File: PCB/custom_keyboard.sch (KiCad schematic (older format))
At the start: 401 parts, among them J1 Conn_01x08_Male, SW1 M1, SW10 LSHIFT, SW11 LCTRL, SW12 1, SW13 Q, SW14 A, SW15 Z, SW16 LGUI, SW17 F1, SW18 2, SW19 W, SW2 M2, SW20 S, SW21 X, SW22 LALT, SW23 F2, SW24 3, SW25 E, SW26 D, SW27 C, SW28 F3, SW29 4, SW3 M3, SW30 R, SW31 F, SW32 V, SW33 F4, SW34 5, SW35 T, SW36 G, SW37 B, SW38 SPACE, SW39 F5, SW4 M4, SW40 6, SW41 Y, SW42 H, SW43 N, SW44 F6, SW45 7, SW46 U, SW47 J, SW48 M, SW49 F7, SW5 M5, SW50 8, SW51 I, SW52 K, SW53 ,/<, SW54 F8, SW55 9, SW56 O, SW57 L, SW58 ./>, SW59 RALT, SW6 ESC, SW60 F9, SW61 0, SW62 P, SW63 ;/:, SW64 /, SW65 RGUI, SW66 F10, SW67 -/_, SW68 [/{, SW69 '/\", SW7 `/~, SW70 CherryMX, SW71 F11, SW72 =/+, SW73 ]/}, SW74 MENU, SW75 F12, SW76 BACKSPACE, SW77 \\, SW78 ENTER, SW79 RSHIFT, SW8 TAB, SW80 RCTRL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

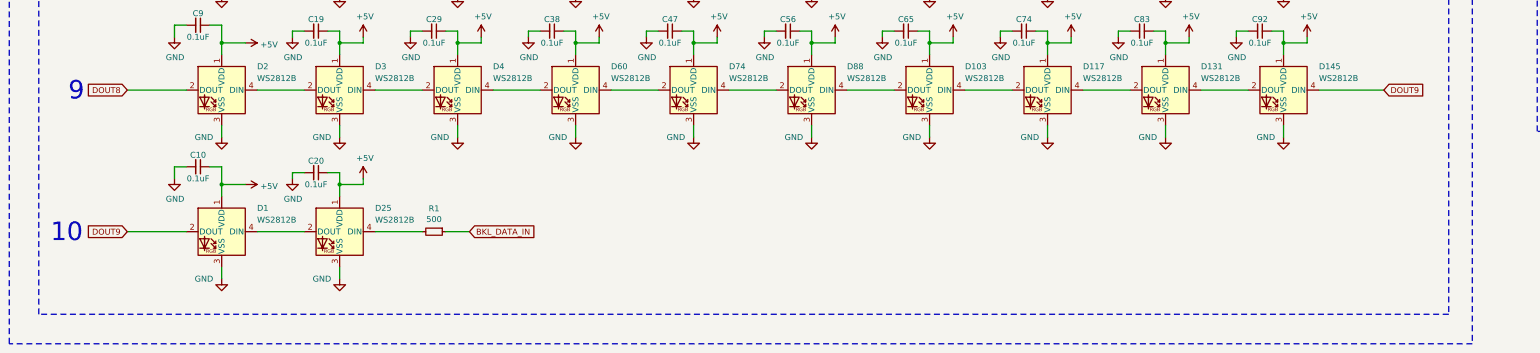
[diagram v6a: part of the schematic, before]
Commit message: Removed unnecessary lighting
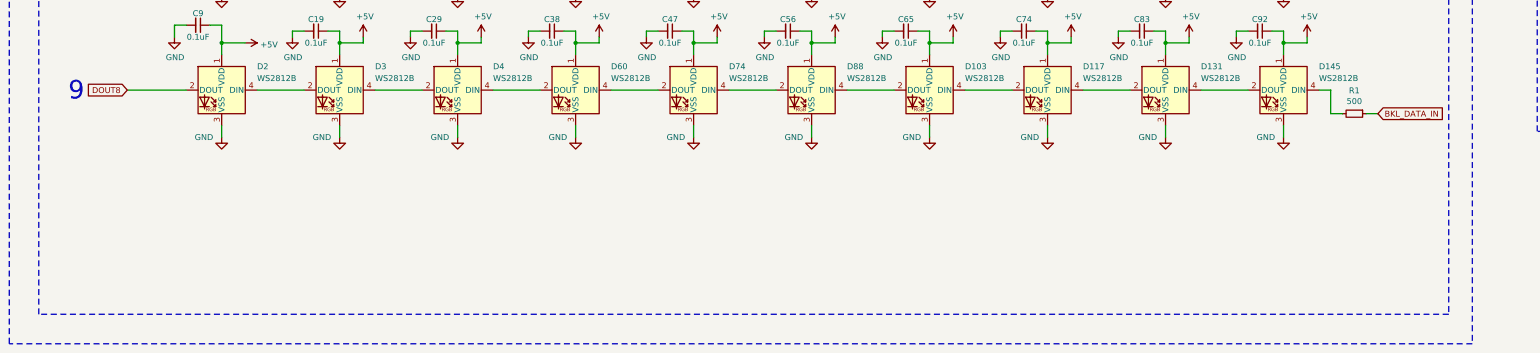
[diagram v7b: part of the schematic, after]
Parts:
- removed C10, C20: 0.1uF, symbol Device:C_Small
- removed D1, D25: WS2812B, LED_SMD:LED_WS2812B_PLCC4_5.0x5.0mm_P3.2mm, symbol LED:WS2812B
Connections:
- net DOUT9 is gone; now on an unnamed net: D145.4 (DIN)
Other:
- moved on the sheet: R1
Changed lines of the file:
@@
 Wire Notes Line
 	1200 7750 1200 1700
-Wire Wire Line
-	4450 19900 4050 19900
-Wire Wire Line
-	4850 19900 4650 19900
 $Comp
 L Device:R_Small R1
 U 1 1 68D631B8
-P 4550 19900
-F 0 "R1" V 4354 19900 50  0000 C CNN
-F 1 "500" V 4445 19900 50  0000 C CNN
-F 2 "" H 4550 19900 50  0001 C CNN
-F 3 "~" H 4550 19900 50  0001 C CNN
-	1    4550 19900
+P 12350 18900
+F 0 "R1" V 12154 18900 50  0000 C CNN
+F 1 "500" V 12245 18900 50  0000 C CNN
+F 2 "" H 12350 18900 50  0001 C CNN
+F 3 "~" H 12350 18900 50  0001 C CNN
+	1    12350 18900
 	0    1    1    0
 $EndComp
-Text GLabel 4850 19900 2    50   Input ~ 0
+Text GLabel 12550 18900 2    50   Input ~ 0
 BKL_DATA_IN
-$Comp
-L power:GND #PWR0397
-U 1 1 68D631C0
-P 3750 20300
-F 0 "#PWR0397" H 3750 20050 50  0001 C CNN
-F 1 "GND" H 3600 20300 50  0000 C CNN
-F 2 "" H 3750 20300 50  0001 C CNN
-F 3 "" H 3750 20300 50  0001 C CNN
-	1    3750 20300
-	1    0    0    -1
-$EndComp
-Wire Wire Line
-	3650 19400 3750 19400
-Wire Wire Line
-	3350 19400 3450 19400
-$Comp
-L Device:C_Small C20
-U 1 1 68D631CC
-P 3550 19400
-F 0 "C20" V 3450 19400 50  0000 C CNN
-F 1 "0.1uF" V 3650 19400 50  0000 C CNN
-F 2 "" H 3550 19400 50  0001 C CNN
-F 3 "~" H 3550 19400 50  0001 C CNN
-	1    3550 19400
-	0    1    1    0
-$EndComp
-$Comp
-L LED:WS2812B D25
-U 1 1 68D631DE
-P 3750 19900
-F 0 "D25" H 3450 20100 50  0000 R CNN
-F 1 "WS2812B" H 3450 20000 50  0000 R CNN
-F 2 "LED_SMD:LED_WS2812B_PLCC4_5.0x5.0mm_P3.2mm" H 3800 19600 50  0001 L TNN
-F 3 "https://cdn-shop.adafruit.com/datasheets/WS2812B.pdf" H 3850 19525 50  0001 L TNN
-	1    3750 19900
-	-1   0    0    -1
-$EndComp
-Text GLabel 1950 19900 0    50   Input ~ 0
-DOUT9
 Text GLabel 1950 18700 0    50   Input ~ 0
 DOUT8
@@
 Text GLabel 1950 10300 0    50   Input ~ 0
 DOUT1
-Text GLabel 12600 18700 2    50   Input ~ 0
-DOUT9
 Text GLabel 12600 17500 2    50   Input ~ 0
 DOUT8
@@
 Text Notes 1450 18800 0    157  ~ 0
 9
-Text Notes 1300 20000 0    157  ~ 0
-10\n
 Text Notes 2650 8300 0    157  ~ 0
 1
@@
 	17950 14750 17450 14750
 Wire Wire Line
-	17450 14850 17950 14850
-Wire Wire Line
-	17950 14950 17450 14950
-Wire Wire Line
-	17450 15050 17950 15050
-Wire Wire Line
-	17950 15150 17450 15150
-Wire Wire Line
 	17950 15350 17450 15350
 Wire Wire Line
@@
 Wire Wire Line
 	17450 15750 17950 15750
-Wire Wire Line
-	17950 16250 17450 16250
-Wire Wire Line
-	17450 16350 17950 16350
-Wire Wire Line
-	17450 16450 17950 16450
-Wire Wire Line
-	17950 16550 17450 16550
-Wire Wire Line
-	17450 16650 17950 16650
-Wire Wire Line
-	17950 16750 17450 16750
-Wire Wire Line
-	17450 16850 17950 16850
-Wire Wire Line
-	17950 16950 17450 16950
-Wire Wire Line
-	17950 17550 17450 17550
-Wire Wire Line
-	17450 17650 17950 17650
-Wire Wire Line
-	17950 17750 17450 17750
-Wire Wire Line
-	17450 17850 17950 17850
-Wire Wire Line
-	15900 17650 16250 17650
-Wire Wire Line
-	16250 17550 15900 17550
-Wire Wire Line
-	15900 17450 16250 17450
-Wire Wire Line
-	16250 17350 15900 17350
-Wire Wire Line
-	15900 17250 16250 17250
-Wire Wire Line
-	16250 17150 15900 17150
 Wire Notes Line
 	13900 19050 13900 8550
@@
 NoConn ~ 15100 16550
 NoConn ~ 15100 16650
-Wire Wire Line
-	3750 20200 3750 20300
 $Comp
 L power:GND #PWR0118
@@
 	1    0    0    -1
 $EndComp
-$Comp
-L power:GND #PWR0124
-U 1 1 8D4BB3A3
-P 3350 19450
-F 0 "#PWR0124" H 3350 19200 50  0001 C CNN
-F 1 "GND" H 3355 19277 50  0000 C CNN
-F 2 "" H 3350 19450 50  0001 C CNN
-F 3 "" H 3350 19450 50  0001 C CNN
-	1    3350 19450
-	1    0    0    -1
-$EndComp
-Wire Wire Line
-	3450 19900 3050 19900
-$Comp
-L power:GND #PWR0125
-U 1 1 8D5D79E1
-P 2750 20300
-F 0 "#PWR0125" H 2750 20050 50  0001 C CNN
-F 1 "GND" H 2600 20300 50  0000 C CNN
-F 2 "" H 2750 20300 50  0001 C CNN
-F 3 "" H 2750 20300 50  0001 C CNN
-	1    2750 20300
-	1    0    0    -1
-$EndComp
-$Comp
-L Device:C_Small C10
-U 1 1 8D5D79ED
-P 2550 19350
-F 0 "C10" V 2450 19350 50  0000 C CNN
-F 1 "0.1uF" V 2650 19350 50  0000 C CNN
-F 2 "" H 2550 19350 50  0001 C CNN
-F 3 "~" H 2550 19350 50  0001 C CNN
-	1    2550 19350
-	0    1    1    0
-$EndComp
-$Comp
-L LED:WS2812B D1
-U 1 1 8D5D79F7
-P 2750 19900
-F 0 "D1" H 2450 20100 50  0000 R CNN
-F 1 "WS2812B" H 2450 20000 50  0000 R CNN
-F 2 "LED_SMD:LED_WS2812B_PLCC4_5.0x5.0mm_P3.2mm" H 2800 19600 50  0001 L TNN
-F 3 "https://cdn-shop.adafruit.com/datasheets/WS2812B.pdf" H 2850 19525 50  0001 L TNN
-	1    2750 19900
-	-1   0    0    -1
-$EndComp
-$Comp
-L power:+5V #PWR0126
-U 1 1 8D5D7A01
-P 2950 19500
-F 0 "#PWR0126" H 2950 19350 50  0001 C CNN
-F 1 "+5V" V 2965 19628 50  0000 L CNN
-F 2 "" H 2950 19500 50  0001 C CNN
-F 3 "" H 2950 19500 50  0001 C CNN
-	1    2950 19500
-	0    1    1    0
-$EndComp
-Wire Wire Line
-	2750 20200 2750 20300
 Wire Wire Line
 	16750 13500 16750 14150
-Wire Wire Line
-	2650 19350 2750 19350
-Wire Wire Line
-	2750 19350 2750 19500
-Wire Wire Line
-	2950 19500 2750 19500
-Connection ~ 2750 19500
-Wire Wire Line
-	2750 19500 2750 19600
-Wire Wire Line
-	2450 19350 2350 19350
-Wire Wire Line
-	2350 19350 2350 19450
-$Comp
-L power:GND #PWR0127
-U 1 1 8E1A5FB8
-P 2350 19450
-F 0 "#PWR0127" H 2350 19200 50  0001 C CNN
-F 1 "GND" H 2355 19277 50  0000 C CNN
-F 2 "" H 2350 19450 50  0001 C CNN
-F 3 "" H 2350 19450 50  0001 C CNN
-	1    2350 19450
-	1    0    0    -1
-$EndComp
 $Comp
 L power:GND #PWR0114
@@
 Wire Wire Line
 	16750 18200 16850 18200
-$Comp
-L power:+5V #PWR0128
-U 1 1 8E4829C0
-P 3950 19450
-F 0 "#PWR0128" H 3950 19300 50  0001 C CNN
-F 1 "+5V" H 3965 19623 50  0000 C CNN
-F 2 "" H 3950 19450 50  0001 C CNN
-F 3 "" H 3950 19450 50  0001 C CNN
-	1    3950 19450
-	1    0    0    -1
-$EndComp
-Wire Wire Line
-	3750 19400 3750 19500
-Wire Wire Line
-	3950 19450 3950 19500
-Wire Wire Line
-	3950 19500 3750 19500
-Connection ~ 3750 19500
-Wire Wire Line
-	3750 19500 3750 19600
-Wire Wire Line
-	3350 19450 3350 19400
 Wire Wire Line
 	16000 15200 16000 15250
@@
 $EndComp
 Wire Wire Line
-	1950 19900 2450 19900
-Wire Wire Line
 	4450 18700 4050 18700
 $Comp
@@
 	11350 18250 11350 18200
 Wire Wire Line
-	12600 18700 12050 18700
-Wire Wire Line
 	4450 17500 4050 17500
 $Comp
@@
 	1    0    0    -1
 $EndComp
+Wire Wire Line
+	16250 17150 15900 17150
+Wire Wire Line
+	15900 17250 16250 17250
+Wire Wire Line
+	16250 17350 15900 17350
+Wire Wire Line
+	15900 17450 16250 17450
+Wire Wire Line
+	16250 17550 15900 17550
+Wire Wire Line
+	15900 17650 16250 17650
+Wire Wire Line
+	17950 16950 17450 16950
+Wire Wire Line
+	17450 16850 17950 16850
+Wire Wire Line
+	17950 16750 17450 16750
+Wire Wire Line
+	17450 16650 17950 16650
+Wire Wire Line
+	17950 16550 17450 16550
+Wire Wire Line
+	17450 16450 17950 16450
+Wire Wire Line
+	17450 16350 17950 16350
+Wire Wire Line
+	17950 16250 17450 16250
+Wire Wire Line
+	17450 17850 17950 17850
+Wire Wire Line
+	17950 17750 17450 17750
+Wire Wire Line
+	17450 17650 17950 17650
+Wire Wire Line
+	17950 17550 17450 17550
+Wire Wire Line
+	17950 15150 17450 15150
+Wire Wire Line
+	17450 15050 17950 15050
+Wire Wire Line
+	17950 14950 17450 14950
+Wire Wire Line
+	17450 14850 17950 14850
+Wire Wire Line
+	12050 18700 12150 18700
+Wire Wire Line
+	12150 18700 12150 18900
+Wire Wire Line
+	12450 18900 12550 18900
+Wire Wire Line
+	12150 18900 12250 18900
 $EndSCHEMATC

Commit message: USB Hub Setup
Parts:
- added C? (x2): 22pF, symbol Device:C_Small
- added J?: USB_A, symbol Connector:USB_A
- added R? (x2): 5.1K, symbol Device:R_Small
- added R? (x2): 22, symbol Device:R_Small
- added TP?: VCC, symbol Connector:TestPoint
- added U?: PRTR5V0U2X, symbol random-keyboard-parts:PRTR5V0U2X
- added U?: 24LC02, symbol Memory_EEPROM:24LC02
- added USB?: HRO-TYPE-C-31-M-12, symbol Type-C:HRO-TYPE-C-31-M-12
- added Y?: 12MHz, symbol Device:Crystal_GND24_Small
- C101, C102: value 22pF -> 18pF
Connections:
- net +5V: now also TP?.1, U?.4 (VCC), USB?.11 (VBUS), USB?.2 (VBUS)
- net GND: now also C?.1, C?.1, R?.1, R?.1, U?.1 (A0), U?.1 (GND), U?.2 (A1), U?.3 (A2), U?.4 (GND), USB?.1 (GND), USB?.12 (GND), USB?.13 (SHIELD), Y?.2, Y?.4
- net KEYBOARD_D+: now also IC?.19 (DP1)
- net KEYBOARD_D-: now also IC?.18 (DM1)
- net HUB_PORT4_D-: now reaches IC?.11 (DM4)
- net HUB_PORT4_D+: now reaches IC?.12 (DP4)
- net HUB_PORT3_D-: now reaches IC?.13 (DM3)
- net HUB_PORT3_D+: now reaches IC?.14 (DP3)
- net HUB_PORT2_D-: now reaches IC?.16 (DM2)
- net HUB_PORT2_D+: now reaches IC?.17 (DP2)
- net HUB_SDA: now reaches IC?.2 (TESTJ)
- net HUB_SDA: now also U?.5 (SDA)
- net HUB_XIN: now reaches IC?.22 (XIN)
- net HUB_XIN: now also C?.2, Y?.1
- net HUB_XOUT: now reaches IC?.23 (XOUT)
- net HUB_XOUT: now also C?.2, Y?.3
- net HUB_D-: now reaches IC?.29 (DMU)
- net HUB_D-: now also R?.2
- net HUB_LED1: now reaches IC?.3 (LED1)
- net HUB_LED1: now also U?.6 (SCL)
- net HUB_D+: now reaches IC?.30 (DPU)
- net HUB_D+: now also R?.2
- net HUB_PORT5_D-: now reaches IC?.32 (DM5)
- net HUB_PORT5_D+: now reaches IC?.33 (DP5)
- net HUB_PORT6_D-: now reaches IC?.34 (DM6)
- net HUB_PORT6_D+: now reaches IC?.35 (DP6)
- net HUB_PORT7_D-: now reaches IC?.37 (DM7)
- net HUB_PORT7_D+: now reaches IC?.38 (DP7)
- net HUB_LED2: now reaches IC?.4 (LED2)
- net HUB_LED7: now reaches IC?.46 (LED7)
- net HUB_LED6: now reaches IC?.47 (LED6)
- net HUB_LED5: now reaches IC?.48 (LED5)
- net HUB_LED3: now reaches IC?.5 (LED3)
- net HUB_LED4: now reaches IC?.7 (LED4)
- new net: R?.1, U?.3 (IO2), USB?.5 (DN2), USB?.7 (DN1)
- new net: R?.1, U?.2 (IO1), USB?.6 (DP1), USB?.8 (DP2)
- new net CC1: R?.2, USB?.4 (CC1)
- new net CC2: R?.2, USB?.10 (CC2)
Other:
- note added: "USB Hub"
- moved on the sheet: IC?
